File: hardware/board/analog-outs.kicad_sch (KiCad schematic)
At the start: 37 parts, among them U902 AD5685RxRUZ

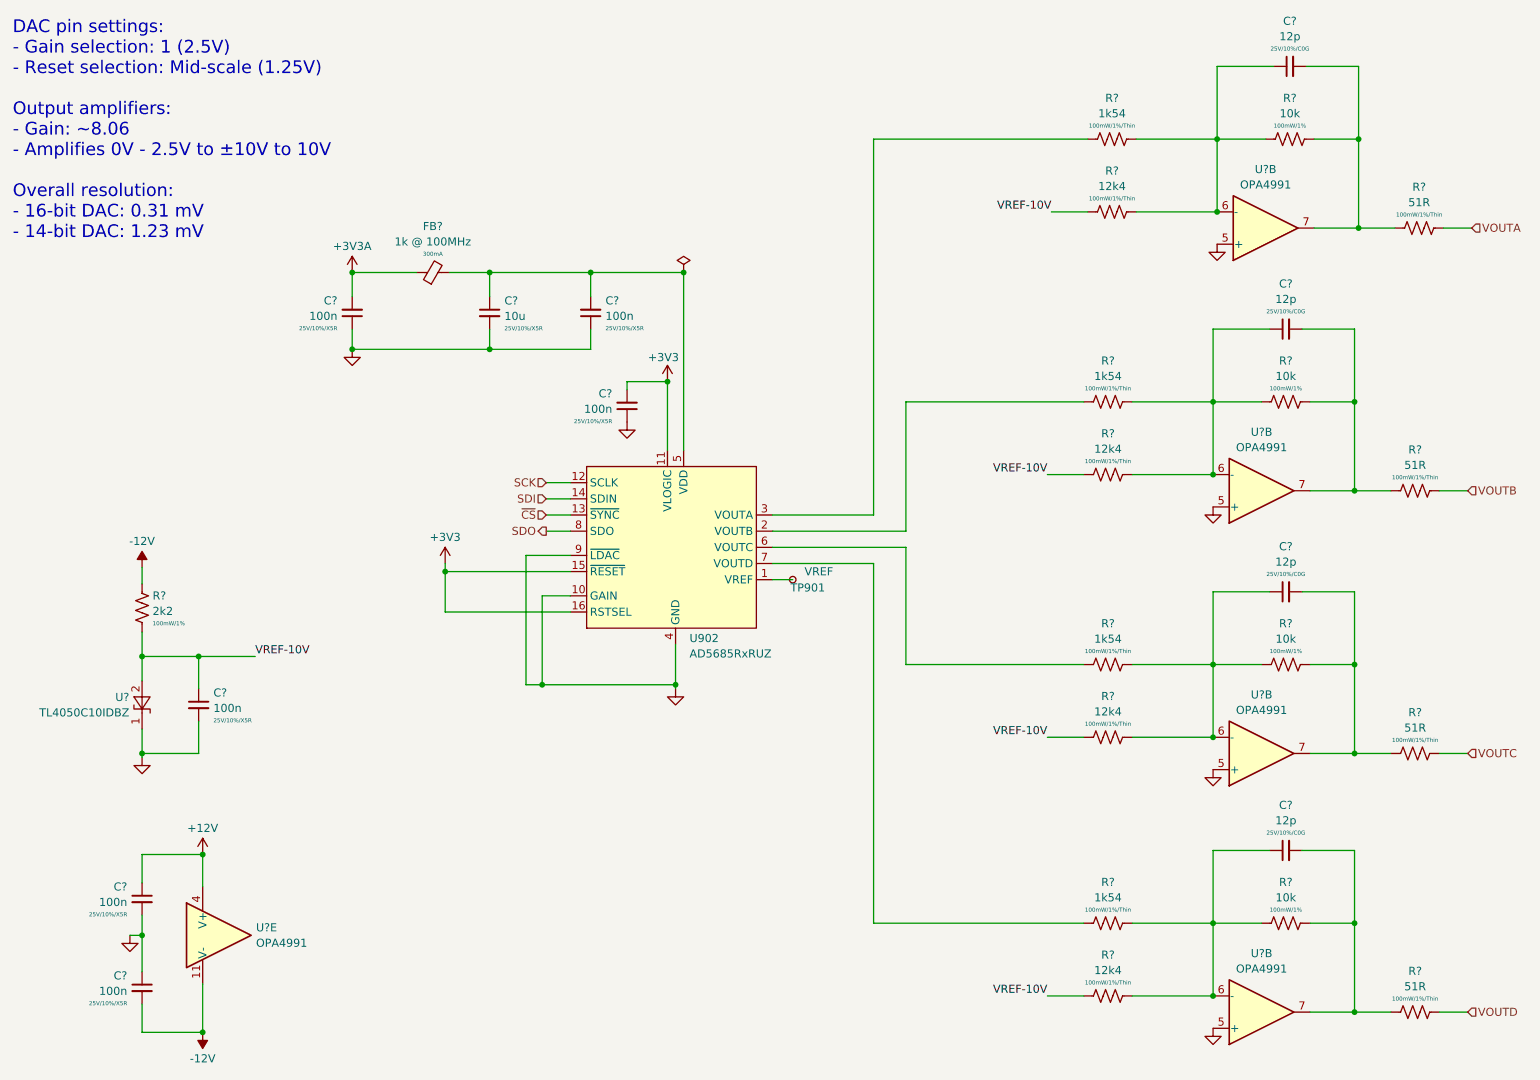
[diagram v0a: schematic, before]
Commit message: Update resistor values in Vout DAC buffers
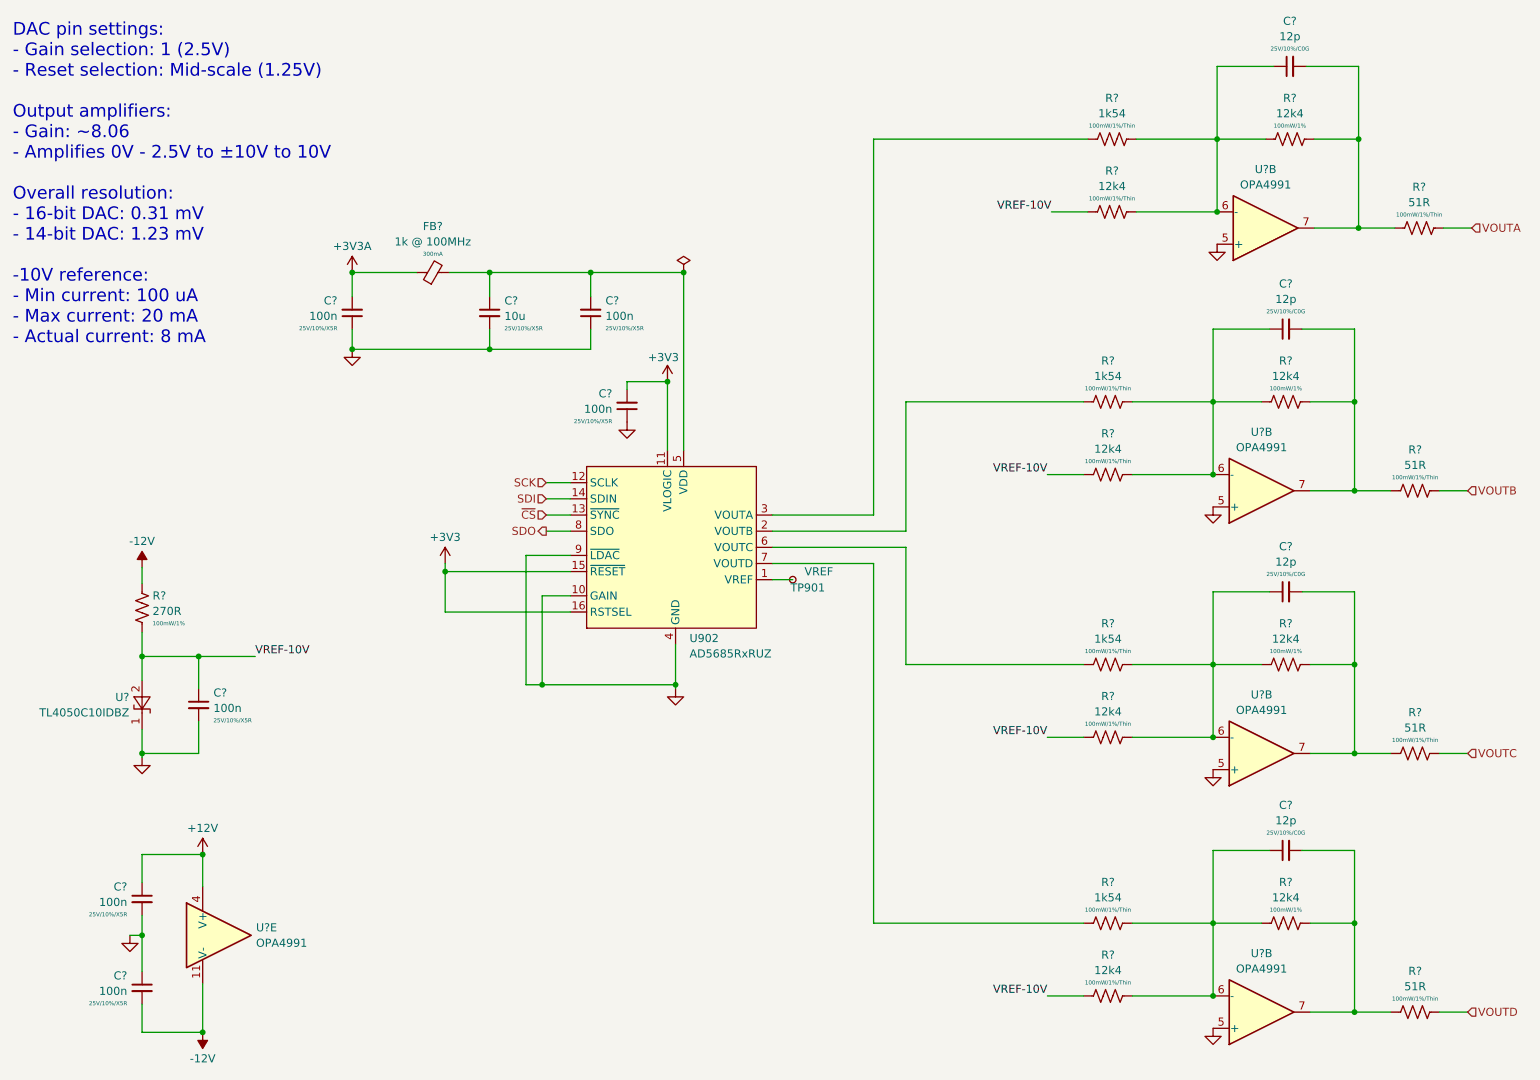
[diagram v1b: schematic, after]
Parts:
- R? (x4): value 10k -> 12k4
- R?: value 2k2 -> 270R
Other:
- note added: "DAC pin settings: - Gain selection: 1 (2.5V) - Reset selection: Mid-scale (1.25V) Output amplifiers: - Gain: ~8.06 - Amplifies 0V - 2.5V to ±10V to 10V Overall resolution: - 16-bit DAC: 0.31 mV - 14-bit DAC: 1.23 mV -10V reference: - Min current: 100 uA - Max current: 20 mA - Actual current: 8 mA"
- note removed: "DAC pin settings: - Gain selection: 1 (2.5V) - Reset selection: Mid-scale (1.25V) Output amplifiers: - Gain: ~8.06 - Amplifies 0V - 2.5V to ±10V to 10V Overall resolution: - 16-bit DAC: 0.31 mV - 14-bit DAC: 1.23 mV"
